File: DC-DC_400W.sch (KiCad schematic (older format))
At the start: 5 parts, among them J1 Conn_01x24, J2 Conn_01x06, J3 Conn_01x10, J4 Conn_01x10

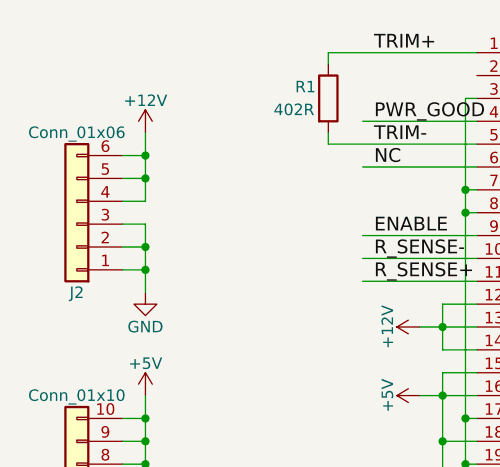
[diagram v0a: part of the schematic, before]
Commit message: move to XT60 connector
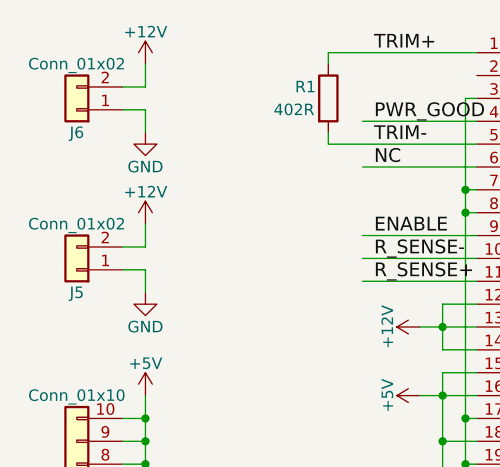
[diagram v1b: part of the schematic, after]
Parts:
- removed J2: Conn_01x06, Connectors_Phoenix:PhoenixContact_MSTBVA-G_06x5.00mm_Vertical, symbol Conn_01x06
- added J5, J6: Conn_01x02, custom:XT60, symbol Conn_01x02
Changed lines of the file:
@@
 LIBS:contrib
 LIBS:valves
+LIBS:DC-DC_400W-cache
 EELAYER 25 0
 EELAYER END
@@
 $EndComp
 $Comp
-L Conn_01x06 J2
-U 1 1 5A3FE714
-P 1900 2950
-F 0 "J2" H 1900 3250 50  0000 C CNN
-F 1 "Conn_01x06" H 1900 2550 50  0000 C CNN
-F 2 "Connectors_Phoenix:PhoenixContact_MSTBVA-G_06x5.00mm_Vertical" H 1900 2950 50  0001 C CNN
-F 3 "" H 1900 2950 50  0001 C CNN
-	1    1900 2950
-	-1   0    0    1
-$EndComp
-$Comp
 L Conn_01x10 J3
 U 1 1 5A3FE814
@@
 	-1   0    0    1
 $EndComp
-$Comp
-L +12V #PWR04
-U 1 1 5A3FEA46
-P 2200 2550
-F 0 "#PWR04" H 2200 2400 50  0001 C CNN
-F 1 "+12V" H 2200 2690 50  0000 C CNN
-F 2 "" H 2200 2550 50  0001 C CNN
-F 3 "" H 2200 2550 50  0001 C CNN
-	1    2200 2550
-	1    0    0    -1
-$EndComp
 Wire Wire Line
 	3000 2200 3650 2200
@@
 Wire Wire Line
 	3000 2600 3000 2550
-Wire Wire Line
-	2100 2650 2200 2650
-Wire Wire Line
-	2200 2550 2200 2850
-Wire Wire Line
-	2200 2750 2100 2750
-Connection ~ 2200 2650
-Wire Wire Line
-	2200 2850 2100 2850
-Connection ~ 2200 2750
-$Comp
-L GND #PWR05
+$Comp
+L GND #PWR04
 U 1 1 5A3FEBAC
 P 2200 6050
-F 0 "#PWR05" H 2200 5800 50  0001 C CNN
+F 0 "#PWR04" H 2200 5800 50  0001 C CNN
 F 1 "GND" H 2200 5900 50  0000 C CNN
 F 2 "" H 2200 6050 50  0001 C CNN
@@
 $EndComp
 $Comp
-L GND #PWR06
-U 1 1 5A3FEBE4
+L +5V #PWR05
+U 1 1 5A3FEF18
+P 2200 3700
+F 0 "#PWR05" H 2200 3550 50  0001 C CNN
+F 1 "+5V" H 2200 3840 50  0000 C CNN
+F 2 "" H 2200 3700 50  0001 C CNN
+F 3 "" H 2200 3700 50  0001 C CNN
+	1    2200 3700
+	1    0    0    -1
+$EndComp
+Wire Wire Line
+	2100 3800 2200 3800
+Wire Wire Line
+	2200 3700 2200 4700
+Wire Wire Line
+	2200 3900 2100 3900
+Connection ~ 2200 3800
+Wire Wire Line
+	2200 4000 2100 4000
+Connection ~ 2200 3900
+Wire Wire Line
+	2200 4100 2100 4100
+Connection ~ 2200 4000
+Wire Wire Line
+	2200 4200 2100 4200
+Connection ~ 2200 4100
+Wire Wire Line
+	2200 4300 2100 4300
+Connection ~ 2200 4200
+Wire Wire Line
+	2200 4400 2100 4400
+Connection ~ 2200 4300
+Wire Wire Line
+	2200 4500 2100 4500
+Connection ~ 2200 4400
+Wire Wire Line
+	2200 4600 2100 4600
+Connection ~ 2200 4500
+Wire Wire Line
+	2200 4700 2100 4700
+Connection ~ 2200 4600
+Wire Wire Line
+	2100 5050 2200 5050
+Wire Wire Line
+	2200 5050 2200 6050
+Wire Wire Line
+	2100 5950 2200 5950
+Connection ~ 2200 5950
+Wire Wire Line
+	2100 5850 2200 5850
+Connection ~ 2200 5850
+Wire Wire Line
+	2100 5750 2200 5750
+Connection ~ 2200 5750
+Wire Wire Line
+	2100 5650 2200 5650
+Connection ~ 2200 5650
+Wire Wire Line
+	2100 5150 2200 5150
+Connection ~ 2200 5150
+Wire Wire Line
+	2100 5250 2200 5250
+Connection ~ 2200 5250
+Wire Wire Line
+	2100 5350 2200 5350
+Connection ~ 2200 5350
+Wire Wire Line
+	2100 5450 2200 5450
+Connection ~ 2200 5450
+Wire Wire Line
+	2100 5550 2200 5550
+Connection ~ 2200 5550
+$Comp
+L Conn_01x02 J5
+U 1 1 5A4F8315
+P 1900 3150
+F 0 "J5" H 1900 3250 50  0000 C CNN
+F 1 "Conn_01x02" H 1900 2950 50  0000 C CNN
+F 2 "custom:XT60" H 1900 3150 50  0001 C CNN
+F 3 "" H 1900 3150 50  0001 C CNN
+	1    1900 3150
+	-1   0    0    1
+$EndComp
+$Comp
+L Conn_01x02 J6
+U 1 1 5A4F84EC
+P 1900 2450
+F 0 "J6" H 1900 2550 50  0000 C CNN
+F 1 "Conn_01x02" H 1900 2250 50  0000 C CNN
+F 2 "custom:XT60" H 1900 2450 50  0001 C CNN
+F 3 "" H 1900 2450 50  0001 C CNN
+	1    1900 2450
+	-1   0    0    1
+$EndComp
+$Comp
+L +12V #PWR06
+U 1 1 5A4F85E8
+P 2200 2250
+F 0 "#PWR06" H 2200 2100 50  0001 C CNN
+F 1 "+12V" H 2200 2390 50  0000 C CNN
+F 2 "" H 2200 2250 50  0001 C CNN
+F 3 "" H 2200 2250 50  0001 C CNN
+	1    2200 2250
+	1    0    0    -1
+$EndComp
+$Comp
+L GND #PWR07
+U 1 1 5A4F8640
 P 2200 3250
-F 0 "#PWR06" H 2200 3000 50  0001 C CNN
+F 0 "#PWR07" H 2200 3000 50  0001 C CNN
 F 1 "GND" H 2200 3100 50  0000 C CNN
 F 2 "" H 2200 3250 50  0001 C CNN
@@
 	1    0    0    -1
 $EndComp
-Wire Wire Line
-	2100 2950 2200 2950
-Wire Wire Line
-	2200 2950 2200 3250
+$Comp
+L GND #PWR08
+U 1 1 5A4F8A4D
+P 2200 2550
+F 0 "#PWR08" H 2200 2300 50  0001 C CNN
+F 1 "GND" H 2200 2400 50  0000 C CNN
+F 2 "" H 2200 2550 50  0001 C CNN
+F 3 "" H 2200 2550 50  0001 C CNN
+	1    2200 2550
+	1    0    0    -1
+$EndComp
+$Comp
+L +12V #PWR09
+U 1 1 5A4F8A6D
+P 2200 2950
+F 0 "#PWR09" H 2200 2800 50  0001 C CNN
+F 1 "+12V" H 2200 3090 50  0000 C CNN
+F 2 "" H 2200 2950 50  0001 C CNN
+F 3 "" H 2200 2950 50  0001 C CNN
+	1    2200 2950
+	1    0    0    -1
+$EndComp
+Wire Wire Line
+	2100 2350 2200 2350
+Wire Wire Line
+	2200 2350 2200 2250
+Wire Wire Line
+	2100 2450 2200 2450
+Wire Wire Line
+	2200 2450 2200 2550
 Wire Wire Line
 	2100 3050 2200 3050
-Connection ~ 2200 3050
+Wire Wire Line
+	2200 3050 2200 2950
 Wire Wire Line
 	2100 3150 2200 3150
-Connection ~ 2200 3150
-$Comp
-L +5V #PWR07
-U 1 1 5A3FEF18
-P 2200 3700
-F 0 "#PWR07" H 2200 3550 50  0001 C CNN
-F 1 "+5V" H 2200 3840 50  0000 C CNN
-F 2 "" H 2200 3700 50  0001 C CNN
-F 3 "" H 2200 3700 50  0001 C CNN
-	1    2200 3700
-	1    0    0    -1
-$EndComp
-Wire Wire Line
-	2100 3800 2200 3800
-Wire Wire Line
-	2200 3700 2200 4700
-Wire Wire Line
-	2200 3900 2100 3900
-Connection ~ 2200 3800
-Wire Wire Line
-	2200 4000 2100 4000
-Connection ~ 2200 3900
-Wire Wire Line
-	2200 4100 2100 4100
-Connection ~ 2200 4000
-Wire Wire Line
-	2200 4200 2100 4200
-Connection ~ 2200 4100
-Wire Wire Line
-	2200 4300 2100 4300
-Connection ~ 2200 4200
-Wire Wire Line
-	2200 4400 2100 4400
-Connection ~ 2200 4300
-Wire Wire Line
-	2200 4500 2100 4500
-Connection ~ 2200 4400
-Wire Wire Line
-	2200 4600 2100 4600
-Connection ~ 2200 4500
-Wire Wire Line
-	2200 4700 2100 4700
-Connection ~ 2200 4600
-Wire Wire Line
-	2100 5050 2200 5050
-Wire Wire Line
-	2200 5050 2200 6050
-Wire Wire Line
-	2100 5950 2200 5950
-Connection ~ 2200 5950
-Wire Wire Line
-	2100 5850 2200 5850
-Connection ~ 2200 5850
-Wire Wire Line
-	2100 5750 2200 5750
-Connection ~ 2200 5750
-Wire Wire Line
-	2100 5650 2200 5650
-Connection ~ 2200 5650
-Wire Wire Line
-	2100 5150 2200 5150
-Connection ~ 2200 5150
-Wire Wire Line
-	2100 5250 2200 5250
-Connection ~ 2200 5250
-Wire Wire Line
-	2100 5350 2200 5350
-Connection ~ 2200 5350
-Wire Wire Line
-	2100 5450 2200 5450
-Connection ~ 2200 5450
-Wire Wire Line
-	2100 5550 2200 5550
-Connection ~ 2200 5550
+Wire Wire Line
+	2200 3150 2200 3250
 $EndSCHEMATC

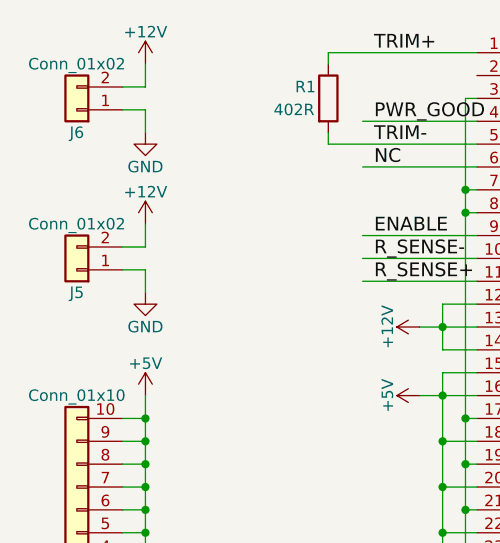
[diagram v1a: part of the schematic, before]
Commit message: remove unused XT60 connector, shrink pcb
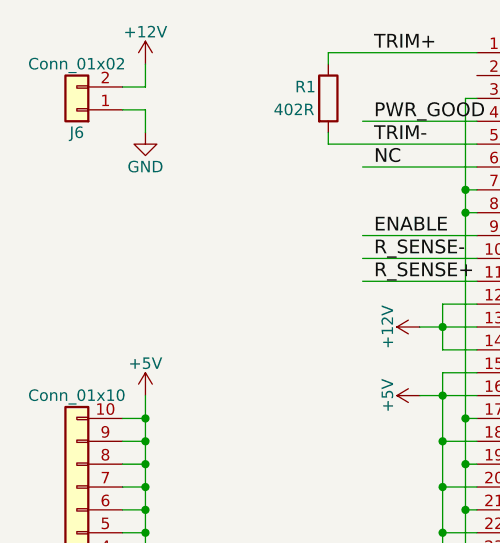
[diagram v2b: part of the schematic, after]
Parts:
- removed J5: Conn_01x02, custom:XT60, symbol Conn_01x02
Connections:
- wire segments 58 -> 54
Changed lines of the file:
@@
 Connection ~ 2200 5550
-$Comp
-L Conn_01x02 J5
-U 1 1 5A4F8315
-P 1900 3150
-F 0 "J5" H 1900 3250 50  0000 C CNN
-F 1 "Conn_01x02" H 1900 2950 50  0000 C CNN
-F 2 "custom:XT60" H 1900 3150 50  0001 C CNN
-F 3 "" H 1900 3150 50  0001 C CNN
-	1    1900 3150
-	-1   0    0    1
-$EndComp
 $Comp
 L Conn_01x02 J6
@@
 $Comp
 L GND #PWR07
-U 1 1 5A4F8640
-P 2200 3250
-F 0 "#PWR07" H 2200 3000 50  0001 C CNN
-F 1 "GND" H 2200 3100 50  0000 C CNN
-F 2 "" H 2200 3250 50  0001 C CNN
-F 3 "" H 2200 3250 50  0001 C CNN
-	1    2200 3250
-	1    0    0    -1
-$EndComp
-$Comp
-L GND #PWR08
 U 1 1 5A4F8A4D
 P 2200 2550
-F 0 "#PWR08" H 2200 2300 50  0001 C CNN
+F 0 "#PWR07" H 2200 2300 50  0001 C CNN
 F 1 "GND" H 2200 2400 50  0000 C CNN
 F 2 "" H 2200 2550 50  0001 C CNN
 F 3 "" H 2200 2550 50  0001 C CNN
 	1    2200 2550
-	1    0    0    -1
-$EndComp
-$Comp
-L +12V #PWR09
-U 1 1 5A4F8A6D
-P 2200 2950
-F 0 "#PWR09" H 2200 2800 50  0001 C CNN
-F 1 "+12V" H 2200 3090 50  0000 C CNN
-F 2 "" H 2200 2950 50  0001 C CNN
-F 3 "" H 2200 2950 50  0001 C CNN
-	1    2200 2950
 	1    0    0    -1
 $EndComp
@@
 Wire Wire Line
 	2200 2450 2200 2550
-Wire Wire Line
-	2100 3050 2200 3050
-Wire Wire Line
-	2200 3050 2200 2950
-Wire Wire Line
-	2100 3150 2200 3150
-Wire Wire Line
-	2200 3150 2200 3250
 $EndSCHEMATC

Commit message: some progress on pcb
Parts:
- added J2: Conn_01x03, Connectors:Fan_Pin_Header_Straight_1x03, symbol Conn_01x03
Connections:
- wire segments 54 -> 58
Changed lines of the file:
@@
 Wire Wire Line
 	2200 2450 2200 2550
+$Comp
+L Conn_01x03 J2
+U 1 1 5A58C05E
+P 1900 1300
+F 0 "J2" H 1900 1500 50  0000 C CNN
+F 1 "Conn_01x03" H 1900 1100 50  0000 C CNN
+F 2 "Connectors:Fan_Pin_Header_Straight_1x03" H 1900 1300 50  0001 C CNN
+F 3 "" H 1900 1300 50  0001 C CNN
+	1    1900 1300
+	-1   0    0    1
+$EndComp
+$Comp
+L GND #PWR?
+U 1 1 5A58C603
+P 2200 1500
+F 0 "#PWR?" H 2200 1250 50  0001 C CNN
+F 1 "GND" H 2200 1350 50  0000 C CNN
+F 2 "" H 2200 1500 50  0001 C CNN
+F 3 "" H 2200 1500 50  0001 C CNN
+	1    2200 1500
+	1    0    0    -1
+$EndComp
+$Comp
+L +12V #PWR?
+U 1 1 5A58C626
+P 2200 1100
+F 0 "#PWR?" H 2200 950 50  0001 C CNN
+F 1 "+12V" H 2200 1240 50  0000 C CNN
+F 2 "" H 2200 1100 50  0001 C CNN
+F 3 "" H 2200 1100 50  0001 C CNN
+	1    2200 1100
+	1    0    0    -1
+$EndComp
+Wire Wire Line
+	2100 1300 2200 1300
+Wire Wire Line
+	2200 1300 2200 1100
+Wire Wire Line
+	2100 1400 2200 1400
+Wire Wire Line
+	2200 1400 2200 1500
 $EndSCHEMATC

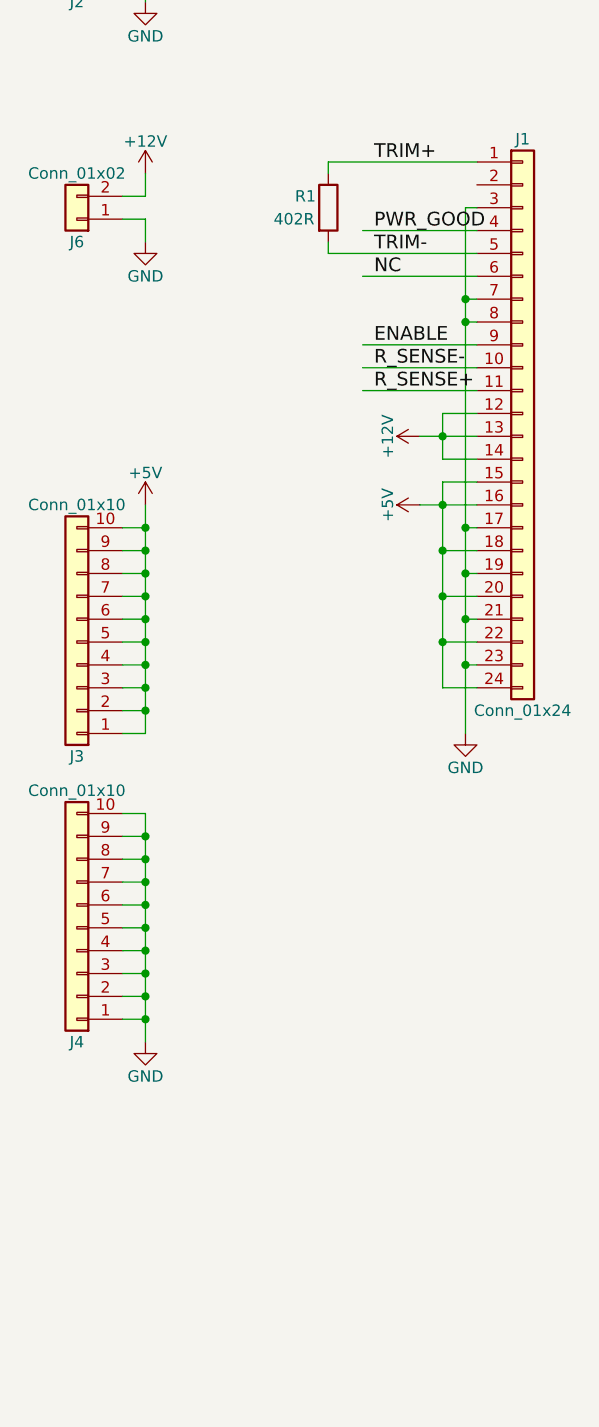
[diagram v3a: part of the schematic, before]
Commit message: gerber generated + pcb fixes
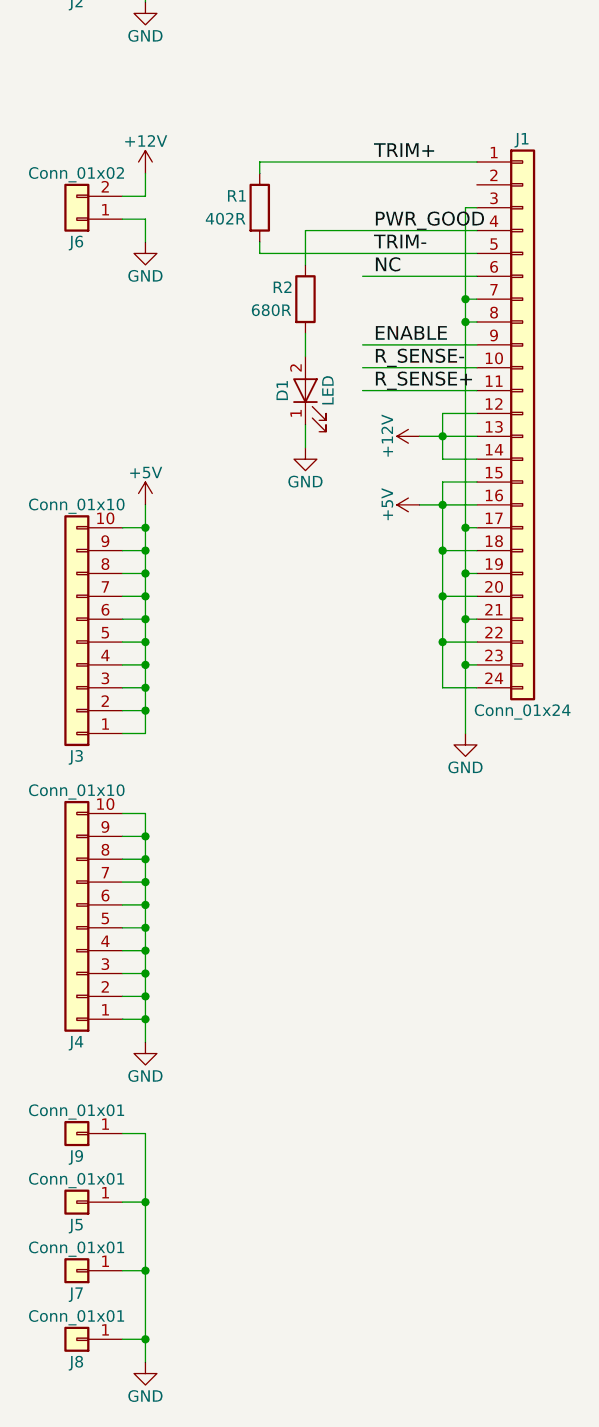
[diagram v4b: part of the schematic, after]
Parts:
- added D1: LED, Diodes_SMD:D_0603, symbol LED
- added J5, J7, J8, J9: Conn_01x01, Mounting_Holes:MountingHole_3.2mm_M3_ISO7380_Pad, symbol Conn_01x01
- added R2: 680R, Resistors_SMD:R_0603, symbol R
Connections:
- wire segments 58 -> 66
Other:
- moved on the sheet: R1
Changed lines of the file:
@@
 L R R1
 U 1 1 5A3FE435
-P 3000 2400
-F 0 "R1" H 2900 2450 50  0000 C CNN
-F 1 "402R" H 2850 2350 50  0000 C CNN
-F 2 "Resistors_SMD:R_0603" V 2930 2400 50  0001 C CNN
-F 3 "" H 3000 2400 50  0001 C CNN
-	1    3000 2400
+P 2700 2400
+F 0 "R1" H 2600 2450 50  0000 C CNN
+F 1 "402R" H 2550 2350 50  0000 C CNN
+F 2 "Resistors_SMD:R_0603" V 2630 2400 50  0001 C CNN
+F 3 "" H 2700 2400 50  0001 C CNN
+	1    2700 2400
 	1    0    0    -1
 $EndComp
@@
 $EndComp
 Wire Wire Line
-	3000 2200 3650 2200
-Wire Wire Line
-	3650 2500 3150 2500
-Wire Wire Line
-	3000 2600 3650 2600
+	2700 2200 3650 2200
+Wire Wire Line
+	2900 2500 3650 2500
+Wire Wire Line
+	2700 2600 3650 2600
 Wire Wire Line
 	3650 2700 3150 2700
@@
 Connection ~ 3600 2800
 Wire Wire Line
-	3000 2200 3000 2250
-Wire Wire Line
-	3000 2600 3000 2550
+	2700 2200 2700 2250
+Wire Wire Line
+	2700 2600 2700 2550
 $Comp
 L GND #PWR04
@@
 $EndComp
 $Comp
-L GND #PWR?
+L GND #PWR08
 U 1 1 5A58C603
 P 2200 1500
-F 0 "#PWR?" H 2200 1250 50  0001 C CNN
+F 0 "#PWR08" H 2200 1250 50  0001 C CNN
 F 1 "GND" H 2200 1350 50  0000 C CNN
 F 2 "" H 2200 1500 50  0001 C CNN
@@
 $EndComp
 $Comp
-L +12V #PWR?
+L +12V #PWR09
 U 1 1 5A58C626
 P 2200 1100
-F 0 "#PWR?" H 2200 950 50  0001 C CNN
+F 0 "#PWR09" H 2200 950 50  0001 C CNN
 F 1 "+12V" H 2200 1240 50  0000 C CNN
 F 2 "" H 2200 1100 50  0001 C CNN
@@
 Wire Wire Line
 	2200 1400 2200 1500
+$Comp
+L R R2
+U 1 1 5A59FEE8
+P 2900 2800
+F 0 "R2" H 2800 2850 50  0000 C CNN
+F 1 "680R" H 2750 2750 50  0000 C CNN
+F 2 "Resistors_SMD:R_0603" V 2830 2800 50  0001 C CNN
+F 3 "" H 2900 2800 50  0001 C CNN
+	1    2900 2800
+	1    0    0    -1
+$EndComp
+$Comp
+L LED D1
+U 1 1 5A59FF6B
+P 2900 3200
+F 0 "D1" H 2900 3300 50  0000 C CNN
+F 1 "LED" H 2900 3100 50  0000 C CNN
+F 2 "Diodes_SMD:D_0603" H 2900 3200 50  0001 C CNN
+F 3 "" H 2900 3200 50  0001 C CNN
+	1    2900 3200
+	0    -1   -1   0
+$EndComp
+$Comp
+L GND #PWR010
+U 1 1 5A5A0040
+P 2900 3450
+F 0 "#PWR010" H 2900 3200 50  0001 C CNN
+F 1 "GND" H 2900 3300 50  0000 C CNN
+F 2 "" H 2900 3450 50  0001 C CNN
+F 3 "" H 2900 3450 50  0001 C CNN
+	1    2900 3450
+	1    0    0    -1
+$EndComp
+Wire Wire Line
+	2900 2950 2900 3050
+Wire Wire Line
+	2900 3350 2900 3450
+Wire Wire Line
+	2900 2650 2900 2500
+$Comp
+L Conn_01x01 J5
+U 1 1 5A5A5FB2
+P 1900 6750
+F 0 "J5" H 1900 6850 50  0000 C CNN
+F 1 "Conn_01x01" H 1900 6650 50  0000 C CNN
+F 2 "Mounting_Holes:MountingHole_3.2mm_M3_ISO7380_Pad" H 1900 6750 50  0001 C CNN
+F 3 "" H 1900 6750 50  0001 C CNN
+	1    1900 6750
+	-1   0    0    1
+$EndComp
+$Comp
+L Conn_01x01 J7
+U 1 1 5A5A61A1
+P 1900 7050
+F 0 "J7" H 1900 7150 50  0000 C CNN
+F 1 "Conn_01x01" H 1900 6950 50  0000 C CNN
+F 2 "Mounting_Holes:MountingHole_3.2mm_M3_ISO7380_Pad" H 1900 7050 50  0001 C CNN
+F 3 "" H 1900 7050 50  0001 C CNN
+	1    1900 7050
+	-1   0    0    1
+$EndComp
+$Comp
+L Conn_01x01 J8
+U 1 1 5A5A61E1
+P 1900 7350
+F 0 "J8" H 1900 7450 50  0000 C CNN
+F 1 "Conn_01x01" H 1900 7250 50  0000 C CNN
+F 2 "Mounting_Holes:MountingHole_3.2mm_M3_ISO7380_Pad" H 1900 7350 50  0001 C CNN
+F 3 "" H 1900 7350 50  0001 C CNN
+	1    1900 7350
+	-1   0    0    1
+$EndComp
+$Comp
+L GND #PWR011
+U 1 1 5A5A623B
+P 2200 7450
+F 0 "#PWR011" H 2200 7200 50  0001 C CNN
+F 1 "GND" H 2200 7300 50  0000 C CNN
+F 2 "" H 2200 7450 50  0001 C CNN
+F 3 "" H 2200 7450 50  0001 C CNN
+	1    2200 7450
+	1    0    0    -1
+$EndComp
+Wire Wire Line
+	2100 6750 2200 6750
+Wire Wire Line
+	2200 6450 2200 7450
+Wire Wire Line
+	2100 7050 2200 7050
+Connection ~ 2200 7050
+Wire Wire Line
+	2100 7350 2200 7350
+Connection ~ 2200 7350
+$Comp
+L Conn_01x01 J9
+U 1 1 5A5A650B
+P 1900 6450
+F 0 "J9" H 1900 6550 50  0000 C CNN
+F 1 "Conn_01x01" H 1900 6350 50  0000 C CNN
+F 2 "Mounting_Holes:MountingHole_3.2mm_M3_ISO7380_Pad" H 1900 6450 50  0001 C CNN
+F 3 "" H 1900 6450 50  0001 C CNN
+	1    1900 6450
+	-1   0    0    1
+$EndComp
+Wire Wire Line
+	2100 6450 2200 6450
+Connection ~ 2200 6750
 $EndSCHEMATC

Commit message: almost done
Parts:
- removed J3, J4: Conn_01x10, Connectors_Phoenix:PhoenixContact_MSTBVA-G_10x5.00mm_Vertical, symbol Conn_01x10
- added J10, J3: Conn_01x05, Connectors_Phoenix:PhoenixContact_MSTBVA-G_05x5.00mm_Vertical, symbol Conn_01x05
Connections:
- wire segments 66 -> 56
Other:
- moved on the sheet: D1, J1, J2, J5, J6, J7, J8, J9, R1, R2

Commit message: final test version
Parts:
- added J4: Conn_01x01, Mounting_Holes:MountingHole_3.2mm_M3_ISO7380_Pad, symbol Conn_01x01
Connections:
- wire segments 56 -> 57
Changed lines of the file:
@@
 $EndComp
 Wire Wire Line
-	5000 4600 5100 4600
-Wire Wire Line
-	5000 4500 5100 4500
-Wire Wire Line
-	5000 4400 5100 4400
+	5100 4600 5000 4600
+Wire Wire Line
+	5100 4500 5000 4500
+Wire Wire Line
+	5100 4400 5000 4400
 Wire Wire Line
 	5000 4300 5100 4300
@@
 L GND #PWR010
 U 1 1 5A5A623B
-P 5100 6250
-F 0 "#PWR010" H 5100 6000 50  0001 C CNN
-F 1 "GND" H 5100 6100 50  0000 C CNN
-F 2 "" H 5100 6250 50  0001 C CNN
-F 3 "" H 5100 6250 50  0001 C CNN
-	1    5100 6250
+P 5100 6600
+F 0 "#PWR010" H 5100 6350 50  0001 C CNN
+F 1 "GND" H 5100 6450 50  0000 C CNN
+F 2 "" H 5100 6600 50  0001 C CNN
+F 3 "" H 5100 6600 50  0001 C CNN
+	1    5100 6600
 	1    0    0    -1
 $EndComp
@@
 	5000 5550 5100 5550
 Wire Wire Line
-	5100 5250 5100 6250
+	5100 5250 5100 6600
 Wire Wire Line
 	5000 5850 5100 5850
@@
 $EndComp
 Wire Wire Line
-	5000 3850 5100 3850
-Wire Wire Line
-	5100 3850 5100 3350
+	5100 3850 5000 3850
+Wire Wire Line
+	5100 3350 5100 3850
 Wire Wire Line
 	5000 3450 5100 3450
@@
 Connection ~ 5100 4400
 Connection ~ 5100 4300
+$Comp
+L Conn_01x01 J4
+U 1 1 5A5DC987
+P 4800 6450
+F 0 "J4" H 4800 6550 50  0000 C CNN
+F 1 "Conn_01x01" H 4800 6350 50  0000 C CNN
+F 2 "Mounting_Holes:MountingHole_3.2mm_M3_ISO7380_Pad" H 4800 6450 50  0001 C CNN
+F 3 "" H 4800 6450 50  0001 C CNN
+	1    4800 6450
+	-1   0    0    1
+$EndComp
+Wire Wire Line
+	5000 6450 5100 6450
+Connection ~ 5100 6450
 $EndSCHEMATC
